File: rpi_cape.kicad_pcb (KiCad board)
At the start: 2 copper layers, 25.4 x 51.8 mm, 2 parts, among them U1 adafruit_DS3231, U2 RPI3B

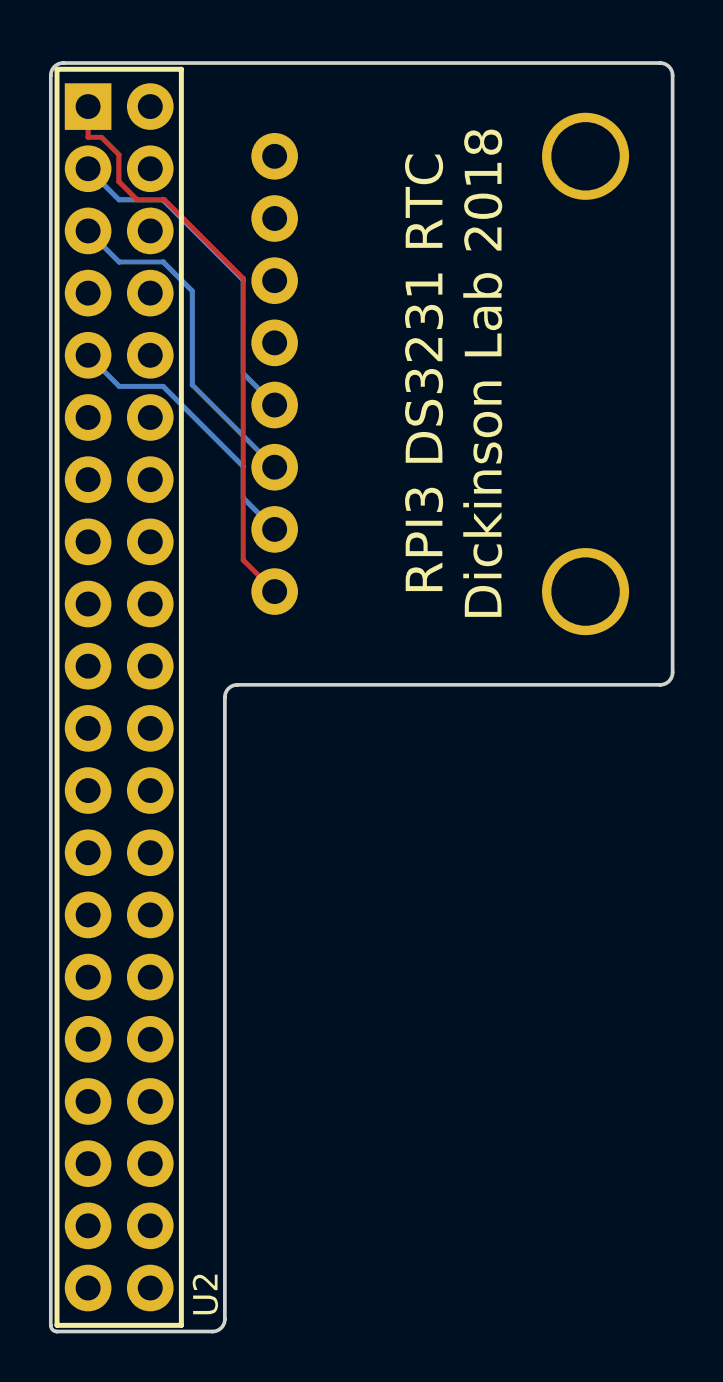
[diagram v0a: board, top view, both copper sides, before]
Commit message: Added dims to layout.
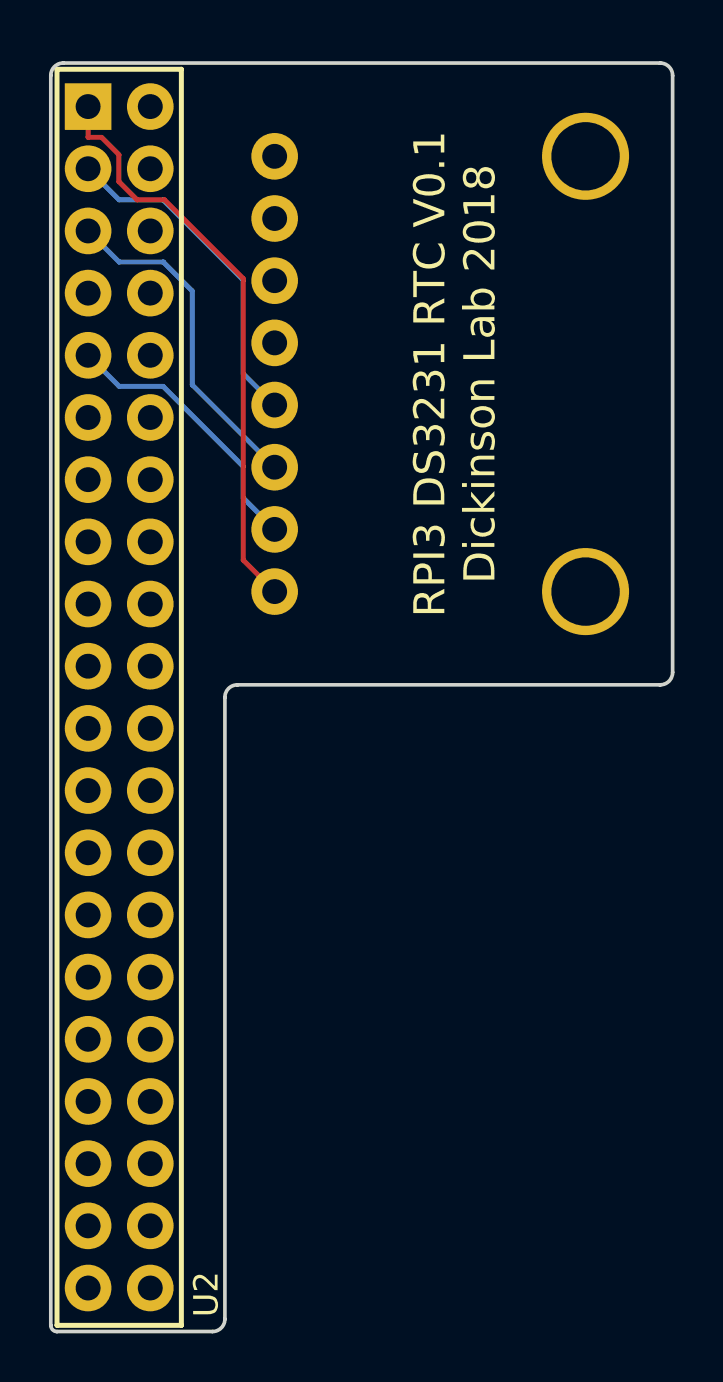
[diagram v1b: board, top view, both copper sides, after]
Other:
- board text added: "RPI3 DS3231 RTC V0.1 Dickinson Lab 2018"
- board text removed: "RPI3 DS3231 RTC Dickinson Lab 2018"
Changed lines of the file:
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@@
     (links 4)
     (no_connects 0)
-    (area 50.724999 50.724999 76.275001 102.691001)
+    (area 40.866288 44.798 76.275001 102.691001)
     (thickness 1.6)
-    (drawings 15)
+    (drawings 17)
     (tracks 24)
     (zones 0)
@@
     (visible_elements FFFFFF7F)
     (pcbplotparams
-      (layerselection 0x00030_80000001)
+      (layerselection 0x010f0_80000001)
       (usegerberextensions false)
       (excludeedgelayer true)
@@
       (outputformat 1)
       (mirror false)
-      (drillshape 1)
+      (drillshape 0)
       (scaleselection 1)
-      (outputdirectory ""))
+      (outputdirectory gerber_v0p1/))
   )
   (net 0 "")
@@
       (net 44 "Net-(U2-Pad40)"))
   )
-  (gr_text "RPI3 DS3231 RTC\nDickinson Lab 2018" (at 67.31 63.5 90) (layer F.SilkS)
-    (effects (font (size 1.5 1.5) (thickness 0.3)))
-  )
   (dimension 25.4 (width 0.3) (layer Dwgs.User)
+    (gr_text "25.400 mm" (at 63.5 38.782) (layer Dwgs.User)
+      (effects (font (size 1.5 1.5) (thickness 0.3)))
+    )
+    (feature1 (pts (xy 76.2 51.308) (xy 76.2 37.432)))
+    (feature2 (pts (xy 50.8 51.308) (xy 50.8 37.432)))
+    (crossbar (pts (xy 50.8 40.132) (xy 76.2 40.132)))
+    (arrow1a (pts (xy 76.2 40.132) (xy 75.073496 40.718421)))
+    (arrow1b (pts (xy 76.2 40.132) (xy 75.073496 39.545579)))
+    (arrow2a (pts (xy 50.8 40.132) (xy 51.926504 40.718421)))
+    (arrow2b (pts (xy 50.8 40.132) (xy 51.926504 39.545579)))
+  )
+  (dimension 51.816 (width 0.3) (layer Dwgs.User)
+    (gr_text "51.816 mm" (at 38.528001 76.708 270) (layer Dwgs.User)
+      (effects (font (size 1.5 1.5) (thickness 0.3)))
+    )
+    (feature1 (pts (xy 50.8 102.616) (xy 37.178001 102.616)))
+    (feature2 (pts (xy 50.8 50.8) (xy 37.178001 50.8)))
+    (crossbar (pts (xy 39.878001 50.8) (xy 39.878001 102.616)))
+    (arrow1a (pts (xy 39.878001 102.616) (xy 39.29158 101.489496)))
+    (arrow1b (pts (xy 39.878001 102.616) (xy 40.464422 101.489496)))
+    (arrow2a (pts (xy 39.878001 50.8) (xy 39.29158 51.926504)))
+    (arrow2b (pts (xy 39.878001 50.8) (xy 40.464422 51.926504)))
+  )
+  (gr_text "RPI3 DS3231 RTC V0.1\nDickinson Lab 2018" (at 67.31 63.5 90) (layer F.SilkS)
+    (effects (font (size 1.27 1.27) (thickness 0.254)))
+  )
+  (dimension 25.4 (width 0.3) (layer Dwgs.User)
